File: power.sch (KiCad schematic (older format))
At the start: 25 parts, among them P24 CONN_2, Q1 MOS_P, Q2 MOS_N, Q3 MOS_P, SW3 SPST, SW4 SPST, U8 MCP73832, U9 MIC5504

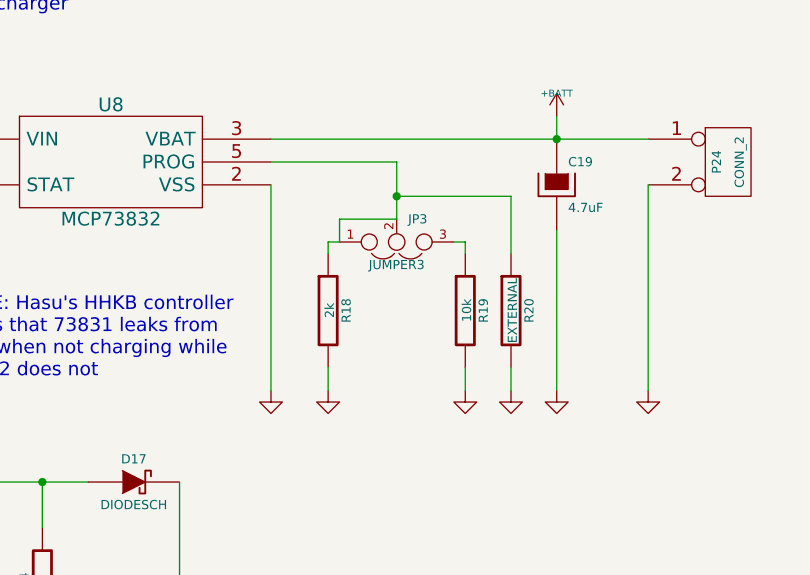
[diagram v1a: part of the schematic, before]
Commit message: Remove most solder jumpers
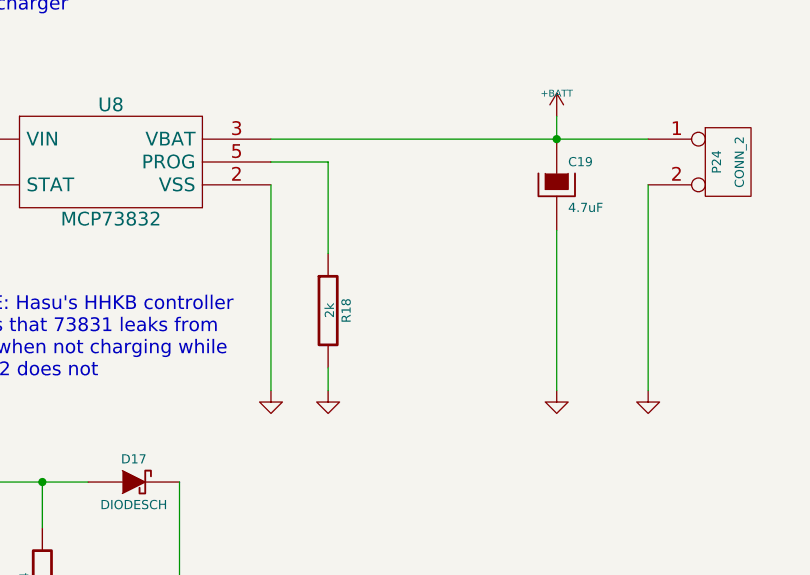
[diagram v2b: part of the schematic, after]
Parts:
- removed JP3: JUMPER3, replacement_kinesis_controller:JUMPER_3, symbol JUMPER3
- removed R19: 10k, Resistors_SMD:R_0805_HandSoldering, symbol R
- removed R20: EXTERNAL, symbol R
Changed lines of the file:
@@
 $EndDescr
 $Comp
-L +5V #PWR57
+L +5V #PWR057
 U 1 1 54E62CDB
 P 1050 1250
-F 0 "#PWR57" H 1050 1340 20  0001 C CNN
+F 0 "#PWR057" H 1050 1340 20  0001 C CNN
 F 1 "+5V" H 1050 1340 30  0000 C CNN
 F 2 "" H 1050 1250 60  0000 C CNN
@@
 $EndComp
 $Comp
-L GND #PWR58
+L GND #PWR058
 U 1 1 54E62CE1
 P 1050 1850
-F 0 "#PWR58" H 1050 1850 30  0001 C CNN
+F 0 "#PWR058" H 1050 1850 30  0001 C CNN
 F 1 "GND" H 1050 1780 30  0001 C CNN
 F 2 "" H 1050 1850 60  0000 C CNN
@@
 $EndComp
 $Comp
-L JUMPER3 JP3
-U 1 1 54E62CFC
-P 4150 1900
-F 0 "JP3" H 4200 1800 40  0000 L CNN
-F 1 "JUMPER3" H 4150 2000 40  0000 C CNN
-F 2 "replacement_kinesis_controller:JUMPER_3" H 4150 1900 60  0001 C CNN
-F 3 "" H 4150 1900 60  0000 C CNN
-	1    4150 1900
-	1    0    0    1
-$EndComp
-$Comp
 L R R18
 U 1 1 54E62D03
@@
 F 3 "" H 3850 2200 30  0000 C CNN
 	1    3850 2200
-	1    0    0    -1
-$EndComp
-$Comp
-L R R19
-U 1 1 54E62D0A
-P 4450 2200
-F 0 "R19" V 4530 2200 40  0000 C CNN
-F 1 "10k" V 4457 2201 40  0000 C CNN
-F 2 "Resistors_SMD:R_0805_HandSoldering" V 4380 2200 30  0001 C CNN
-F 3 "" H 4450 2200 30  0000 C CNN
-	1    4450 2200
-	1    0    0    -1
-$EndComp
-$Comp
-L R R20
-U 1 1 54E62D11
-P 4650 2200
-F 0 "R20" V 4730 2200 40  0000 C CNN
-F 1 "EXTERNAL" V 4657 2201 40  0000 C CNN
-F 2 "" V 4580 2200 30  0001 C CNN
-F 3 "" H 4650 2200 30  0000 C CNN
-	1    4650 2200
 	1    0    0    -1
 $EndComp
@@
 $EndComp
 $Comp
-L GND #PWR64
+L GND #PWR059
 U 1 1 54E62D26
 P 3600 2550
-F 0 "#PWR64" H 3600 2550 30  0001 C CNN
+F 0 "#PWR059" H 3600 2550 30  0001 C CNN
 F 1 "GND" H 3600 2480 30  0001 C CNN
 F 2 "" H 3600 2550 60  0000 C CNN
@@
 $EndComp
 $Comp
-L GND #PWR65
+L GND #PWR060
 U 1 1 54E62D2C
 P 3850 2550
-F 0 "#PWR65" H 3850 2550 30  0001 C CNN
+F 0 "#PWR060" H 3850 2550 30  0001 C CNN
 F 1 "GND" H 3850 2480 30  0001 C CNN
 F 2 "" H 3850 2550 60  0000 C CNN
@@
 $EndComp
 $Comp
-L GND #PWR66
-U 1 1 54E62D32
-P 4450 2550
-F 0 "#PWR66" H 4450 2550 30  0001 C CNN
-F 1 "GND" H 4450 2480 30  0001 C CNN
-F 2 "" H 4450 2550 60  0000 C CNN
-F 3 "" H 4450 2550 60  0000 C CNN
-	1    4450 2550
-	1    0    0    -1
-$EndComp
-$Comp
-L GND #PWR67
-U 1 1 54E62D38
-P 4650 2550
-F 0 "#PWR67" H 4650 2550 30  0001 C CNN
-F 1 "GND" H 4650 2480 30  0001 C CNN
-F 2 "" H 4650 2550 60  0000 C CNN
-F 3 "" H 4650 2550 60  0000 C CNN
-	1    4650 2550
-	1    0    0    -1
-$EndComp
-$Comp
-L GND #PWR69
+L GND #PWR061
 U 1 1 54E62D3E
 P 4850 2550
-F 0 "#PWR69" H 4850 2550 30  0001 C CNN
+F 0 "#PWR061" H 4850 2550 30  0001 C CNN
 F 1 "GND" H 4850 2480 30  0001 C CNN
 F 2 "" H 4850 2550 60  0000 C CNN
@@
 $EndComp
 $Comp
-L +BATT #PWR68
+L +BATT #PWR062
 U 1 1 54E62D44
 P 4850 1350
-F 0 "#PWR68" H 4850 1300 20  0001 C CNN
+F 0 "#PWR062" H 4850 1300 20  0001 C CNN
 F 1 "+BATT" H 4850 1450 30  0000 C CNN
 F 2 "" H 4850 1350 60  0000 C CNN
@@
 $EndComp
 $Comp
-L GND #PWR70
+L GND #PWR063
 U 1 1 54E62D51
 P 5250 2550
-F 0 "#PWR70" H 5250 2550 30  0001 C CNN
+F 0 "#PWR063" H 5250 2550 30  0001 C CNN
 F 1 "GND" H 5250 2480 30  0001 C CNN
 F 2 "" H 5250 2550 60  0000 C CNN
@@
 	3850 2550 3850 2450
 Wire Wire Line
-	4450 2550 4450 2450
-Wire Wire Line
-	4650 2550 4650 2450
-Wire Wire Line
 	4850 2550 4850 1850
 Wire Wire Line
-	3600 1550 4150 1550
-Wire Wire Line
-	4150 1550 4150 1800
-Wire Wire Line
-	3900 1900 3850 1900
-Wire Wire Line
-	3850 1900 3850 1950
-Wire Wire Line
-	4400 1900 4450 1900
-Wire Wire Line
-	4450 1900 4450 1950
-Wire Wire Line
-	4650 1950 4650 1700
-Wire Wire Line
-	4650 1700 4150 1700
-Connection ~ 4150 1700
-Wire Wire Line
-	4150 1800 3900 1800
-Wire Wire Line
-	3900 1800 3900 1900
+	3850 1550 3850 1950
 Wire Wire Line
 	3600 1450 5250 1450
@@
 	3200 6400 3500 6400
 $Comp
-L +BATT #PWR61
+L +BATT #PWR064
 U 1 1 54E64283
 P 2700 5200
-F 0 "#PWR61" H 2700 5150 20  0001 C CNN
+F 0 "#PWR064" H 2700 5150 20  0001 C CNN
 F 1 "+BATT" H 2700 5300 30  0000 C CNN
 F 2 "" H 2700 5200 60  0000 C CNN
@@
 $EndComp
 $Comp
-L GND #PWR63
+L GND #PWR065
 U 1 1 54E64289
 P 3200 7000
-F 0 "#PWR63" H 3200 7000 30  0001 C CNN
+F 0 "#PWR065" H 3200 7000 30  0001 C CNN
 F 1 "GND" H 3200 6930 30  0001 C CNN
 F 2 "" H 3200 7000 60  0000 C CNN
@@
 $EndComp
 $Comp
-L +BATT #PWR59
+L +BATT #PWR066
 U 1 1 54E64297
 P 1100 3900
-F 0 "#PWR59" H 1100 3850 20  0001 C CNN
+F 0 "#PWR066" H 1100 3850 20  0001 C CNN
 F 1 "+BATT" H 1100 4000 30  0000 C CNN
 F 2 "" H 1100 3900 60  0000 C CNN
@@
 $EndComp
 $Comp
-L VCC #PWR71
+L VCC #PWR067
 U 1 1 54E642B2
 P 7050 3900
-F 0 "#PWR71" H 7050 4000 30  0001 C CNN
+F 0 "#PWR067" H 7050 4000 30  0001 C CNN
 F 1 "VCC" H 7050 4000 30  0000 C CNN
 F 2 "" H 7050 3900 60  0000 C CNN
@@
 	800  2950 2800 2950
 $Comp
-L +5V #PWR60
+L +5V #PWR068
 U 1 1 54E642BF
 P 2000 2850
-F 0 "#PWR60" H 2000 2940 20  0001 C CNN
+F 0 "#PWR068" H 2000 2940 20  0001 C CNN
 F 1 "+5V" H 2000 2940 30  0000 C CNN
 F 2 "" H 2000 2850 60  0000 C CNN
@@
 	7050 3900 7050 4100
 $Comp
-L GND #PWR62
+L GND #PWR069
 U 1 1 54E642C9
 P 3200 4650
-F 0 "#PWR62" H 3200 4650 30  0001 C CNN
+F 0 "#PWR069" H 3200 4650 30  0001 C CNN
 F 1 "GND" H 3200 4580 30  0001 C CNN
 F 2 "" H 3200 4650 60  0000 C CNN
@@
 	4900 4100 4900 4500
 Connection ~ 4900 4500
+Wire Wire Line
+	3850 1550 3600 1550
 $EndSCHEMATC

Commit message: More silk updates and another WS2811 breakout
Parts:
- U8, U9: footprint Housings_SOT-23_SOT-143_TSOT-6:SOT23-5 -> replacement_kinesis_controller:SOT23-5_handsolder
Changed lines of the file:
@@
 F 0 "U8" H 2900 1700 60  0000 C CNN
 F 1 "MCP73832" H 2900 1200 60  0000 C CNN
-F 2 "Housings_SOT-23_SOT-143_TSOT-6:SOT23-5" H 2900 1500 60  0001 C CNN
+F 2 "replacement_kinesis_controller:SOT23-5_handsolder" H 2900 1500 60  0001 C CNN
 F 3 "" H 2900 1500 60  0000 C CNN
 	1    2900 1500
@@
 F 0 "U9" H 5750 4250 60  0000 C CNN
 F 1 "MIC5504" H 5750 3750 60  0000 C CNN
-F 2 "Housings_SOT-23_SOT-143_TSOT-6:SOT23-5" H 5750 4050 60  0001 C CNN
+F 2 "replacement_kinesis_controller:SOT23-5_handsolder" H 5750 4050 60  0001 C CNN
 F 3 "" H 5750 4050 60  0000 C CNN
 	1    5750 4050
